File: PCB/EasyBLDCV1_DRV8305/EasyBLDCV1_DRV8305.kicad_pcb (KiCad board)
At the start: 4 copper layers, 66.4 x 43.1 mm, 74 parts, among them J1 10159560-A00221RLF, J2 TC2050-IDC, Q1 CSD16556Q5B, Q2 CSD16556Q5B, Q3 CSD16556Q5B, Q4 CSD16556Q5B, Q5 CSD16556Q5B, Q6 CSD16556Q5B, U1 DRV83053PHP, U2 TMS320F28027FPTT, U3 TPD4E05U06DQAR, U4 LMR16006XDDCR

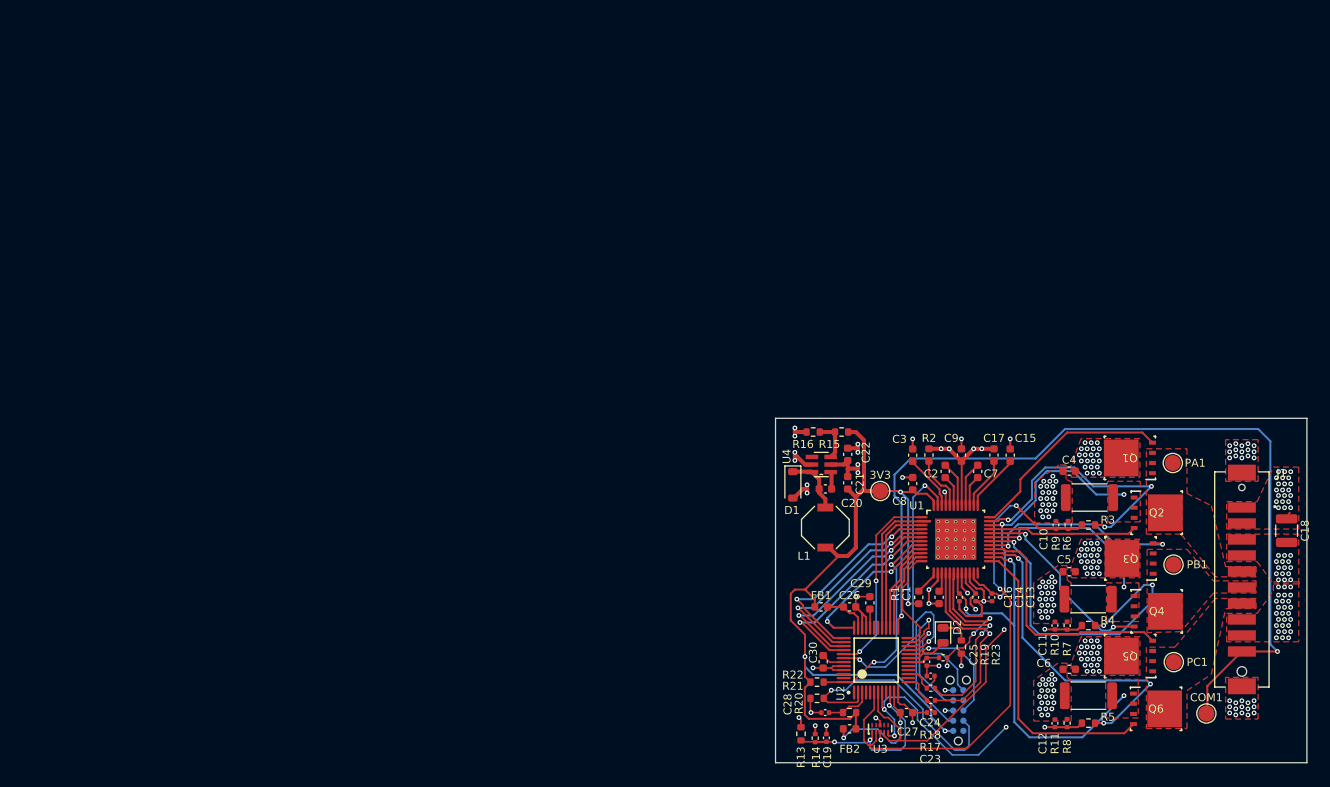
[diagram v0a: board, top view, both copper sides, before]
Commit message: Fixed More DRC started final layout
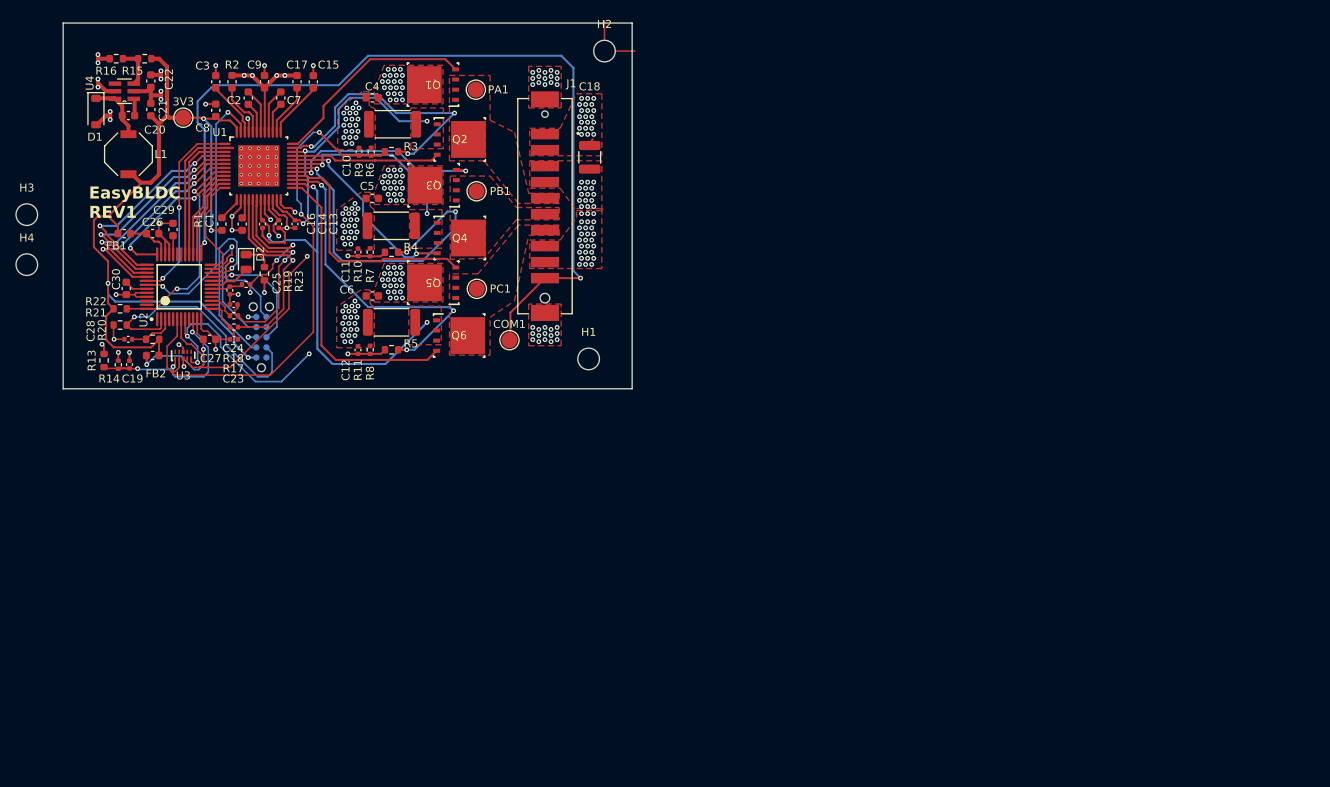
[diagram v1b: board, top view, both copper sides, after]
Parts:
- added H1: M2.5, MountingHole:MountingHole_2.7mm_M2.5_DIN965, F.Cu at (92.6, 70.5)
- added H2: M2.5, MountingHole:MountingHole_2.7mm_M2.5_DIN965, F.Cu at (94.6, 32.0)
- added H3: M2.5, MountingHole:MountingHole_2.7mm_M2.5_DIN965, F.Cu at (22.4, 52.5)
- added H4: M2.5, MountingHole:MountingHole_2.7mm_M2.5_DIN965, F.Cu at (22.4, 58.7)
- moved 3V3 98.8 mm to (41.9, 40.3)
- moved C11 98.8 mm to (63.8, 57.1)
- moved C12 98.8 mm to (63.8, 69.4)
- moved C14 98.8 mm to (53.8, 53.6)
- moved C17 98.8 mm to (58.2, 35.8)
- moved C22 98.8 mm to (37.9, 35.8)
- moved C3 98.8 mm to (46.0, 35.8)
- moved C4 98.8 mm to (65.5, 37.8)
- moved C5 98.8 mm to (65.5, 50.4)
- moved C6 98.8 mm to (65.5, 62.6)
- moved COM1 98.8 mm to (82.7, 68.1)
- moved FB2 98.8 mm to (38.1, 70.1)
- moved J2 98.8 mm to (51.7, 67.8)
- moved L1 98.8 mm to (35.1, 44.9)
- moved PA1 98.8 mm to (78.5, 36.8)
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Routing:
- net GND: track 74.9 -> 76.9 mm, vias 162 -> 163
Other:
- board size 66.4 x 43.1 mm -> 71.1 x 45.7 mm
- board text added: "EasyBLDC REV1"

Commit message: Updated PCB Graphics and Layout
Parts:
- H1, H2, H3, H4: footprint MountingHole:MountingHole_2.7mm_M2.5_DIN965 -> MountingHole:MountingHole_2.7mm_M2.5_ISO7380
- moved H1 74.9 mm to (28.1, 32.4)
- moved H3 72.6 mm to (92.7, 70.4)
- moved H4 13.0 mm to (28.1, 70.4)
- moved C22 3.69 mm to (38.6, 39.4)
- moved C20 3.69 mm to (35.8, 43.7)
- moved C21 3.69 mm to (38.6, 42.9)
- moved D1 3.69 mm to (31.8, 43.2)
- moved L1 3.69 mm to (35.8, 48.5)
- moved R15 3.69 mm to (37.8, 36.6)
- moved R16 3.69 mm to (34.3, 36.6)
- moved U4 3.69 mm to (35.3, 40.6)
- moved H2 1.89 mm to (92.7, 32.4)
- moved 3V3 0.76 mm to (42.7, 40.4)
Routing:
- net 3.3V: track 108.5 -> 105.9 mm
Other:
- board size 71.1 x 45.7 mm -> 72.4 x 45.7 mm

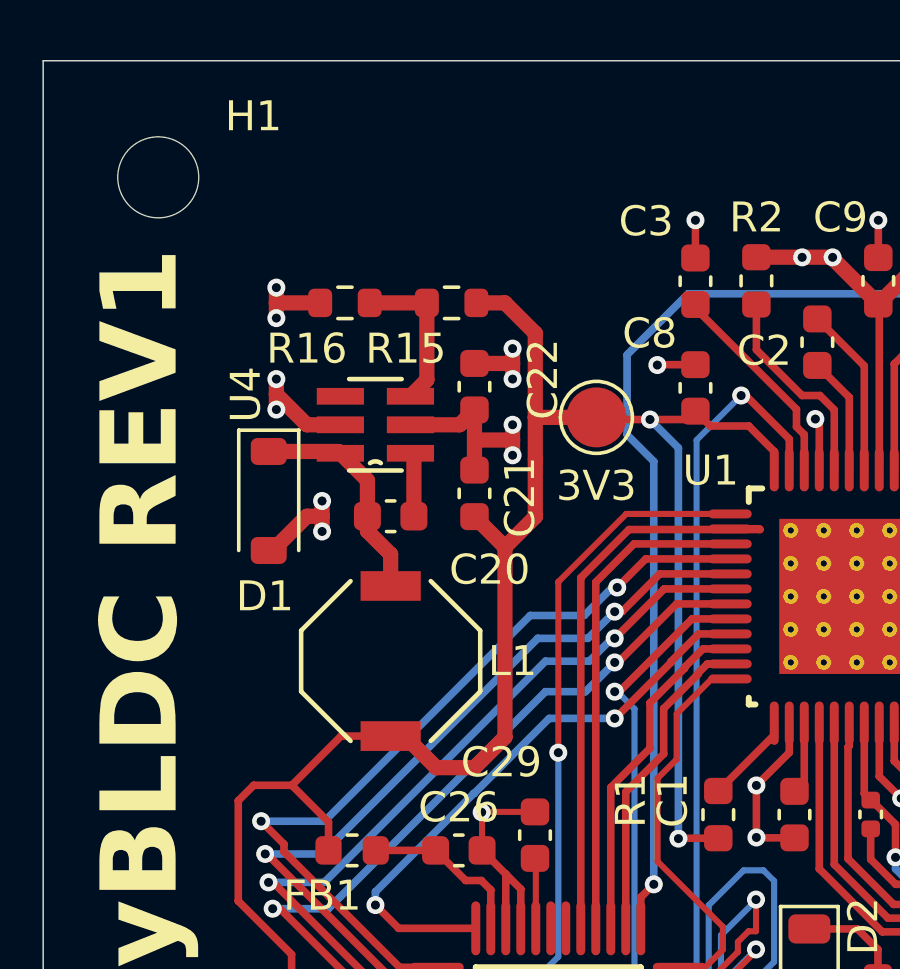
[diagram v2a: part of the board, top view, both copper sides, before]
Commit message: Updated Inductor and excluded tps from BOM
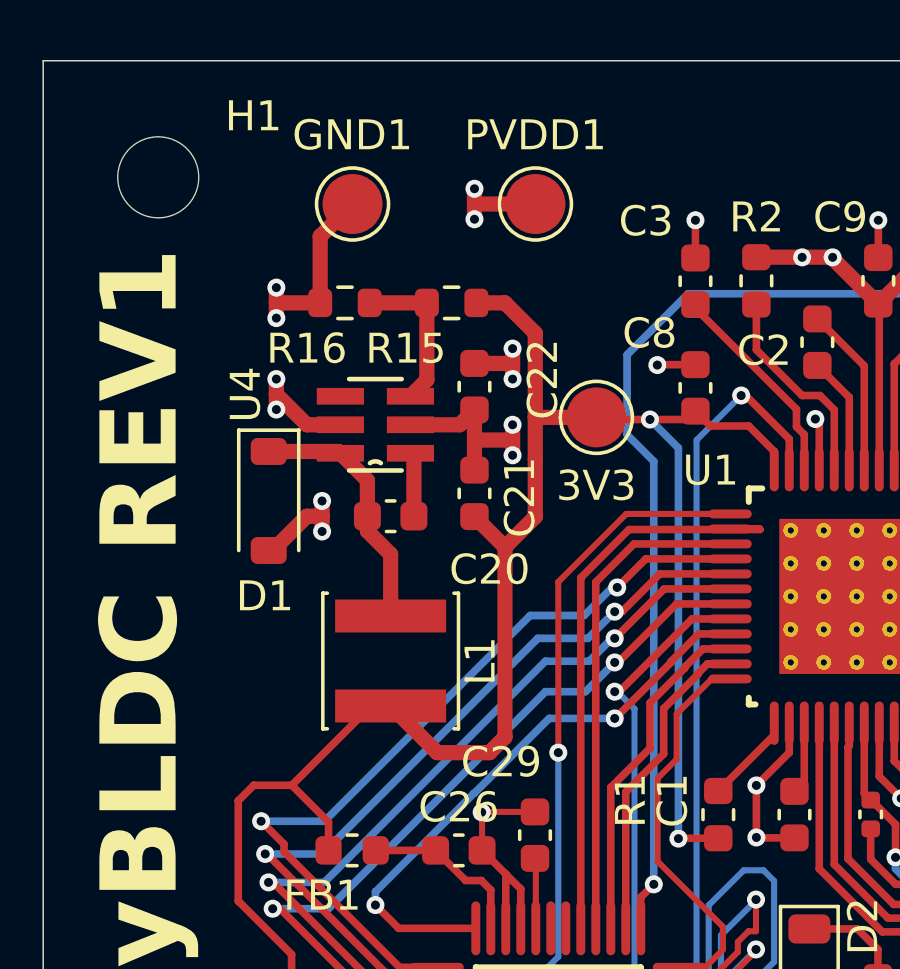
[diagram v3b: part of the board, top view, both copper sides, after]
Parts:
- added GND1: TestPoint, TestPoint:TestPoint_Pad_D2.0mm, F.Cu at (34.5, 33.3)
- added PVDD1: TestPoint, TestPoint:TestPoint_Pad_D2.0mm, F.Cu at (40.6, 33.3)
- L1: footprint EasyBLDC:SD53 -> Inductor_SMD:L_Changjiang_FNR4020S
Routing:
- net GND: track 76.9 -> 80.7 mm
- net PVDD: track 22.4 -> 25.4 mm, vias 93 -> 95
- net Net-(D1-K): track 7.53 -> 8.53 mm

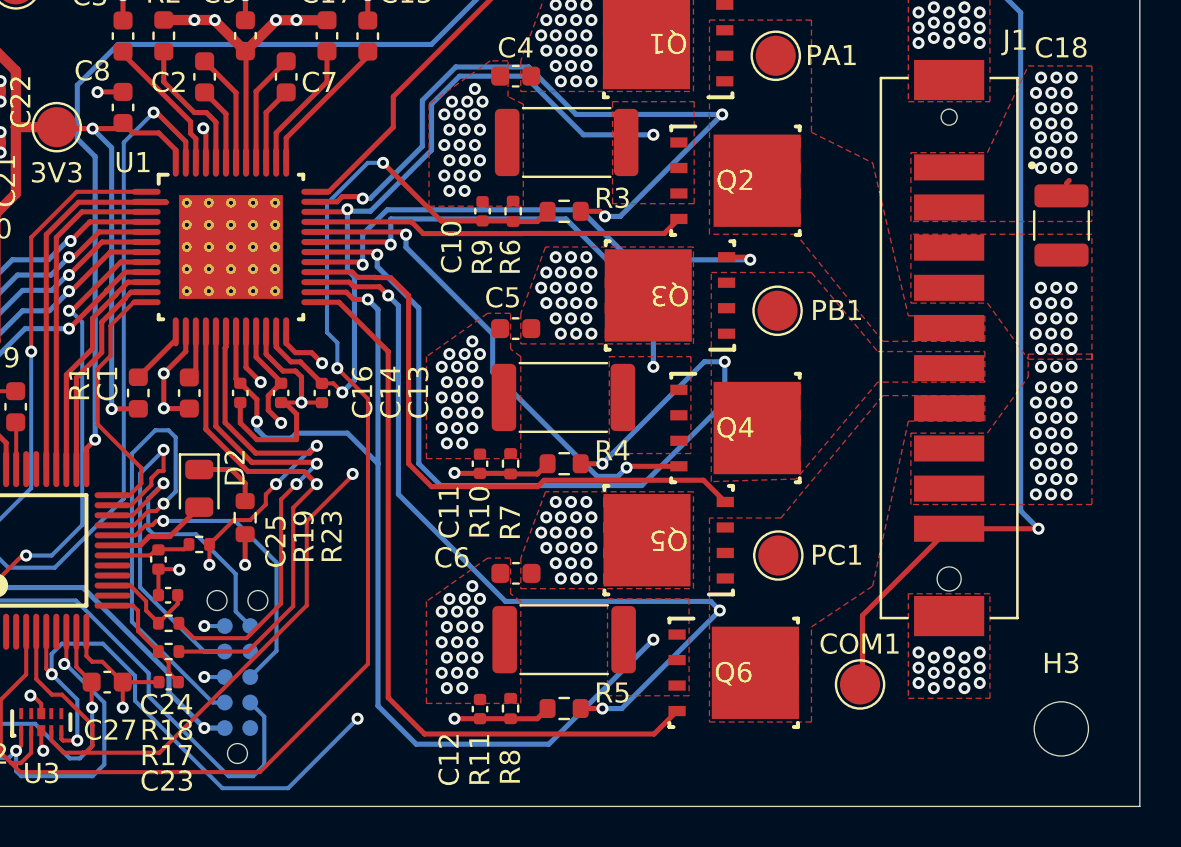
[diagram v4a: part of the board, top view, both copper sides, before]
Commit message: Changed main connector pinout to improve signal integrity
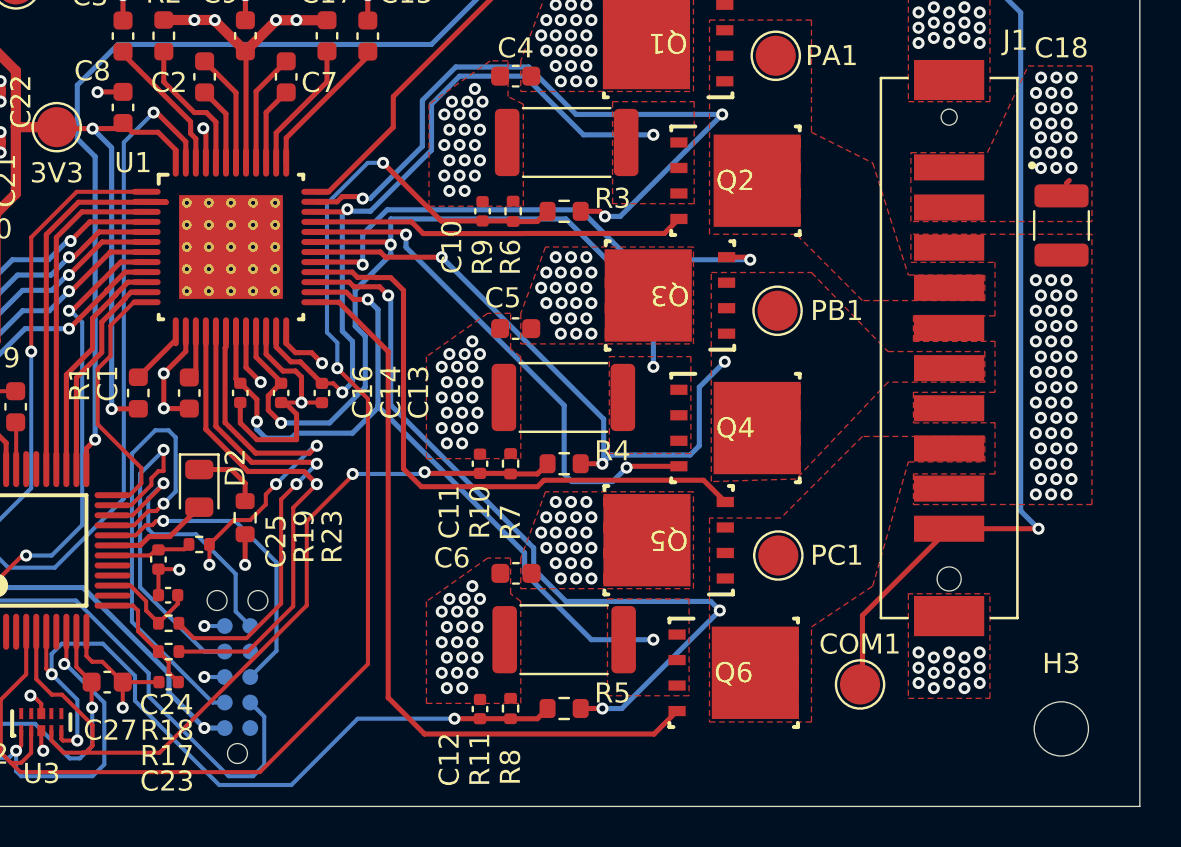
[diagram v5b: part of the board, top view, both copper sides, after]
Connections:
- J1 pad 4: GND -> MOT_A
- J1 pad 5: MOT_A -> GND
- J1 pad 7: MOT_C -> GND
- J1 pad 8: GND -> MOT_C
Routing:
- net SL_C: track 52.1 -> 39.7 mm
- net MOT_B: track 43.1 -> 31.0 mm
- net MOT_C: track 41.4 -> 39.6 mm
- net SL_B: track 42.6 -> 41.5 mm
- net GL_B: track 24.8 -> 25.9 mm
- net VSEN_C: track 38.6 -> 38.4 mm, vias 4 -> 3
- net GND: vias 163 -> 166

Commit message: Fixed Silkscreen DRC Errors
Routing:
- net GND: vias 166 -> 193

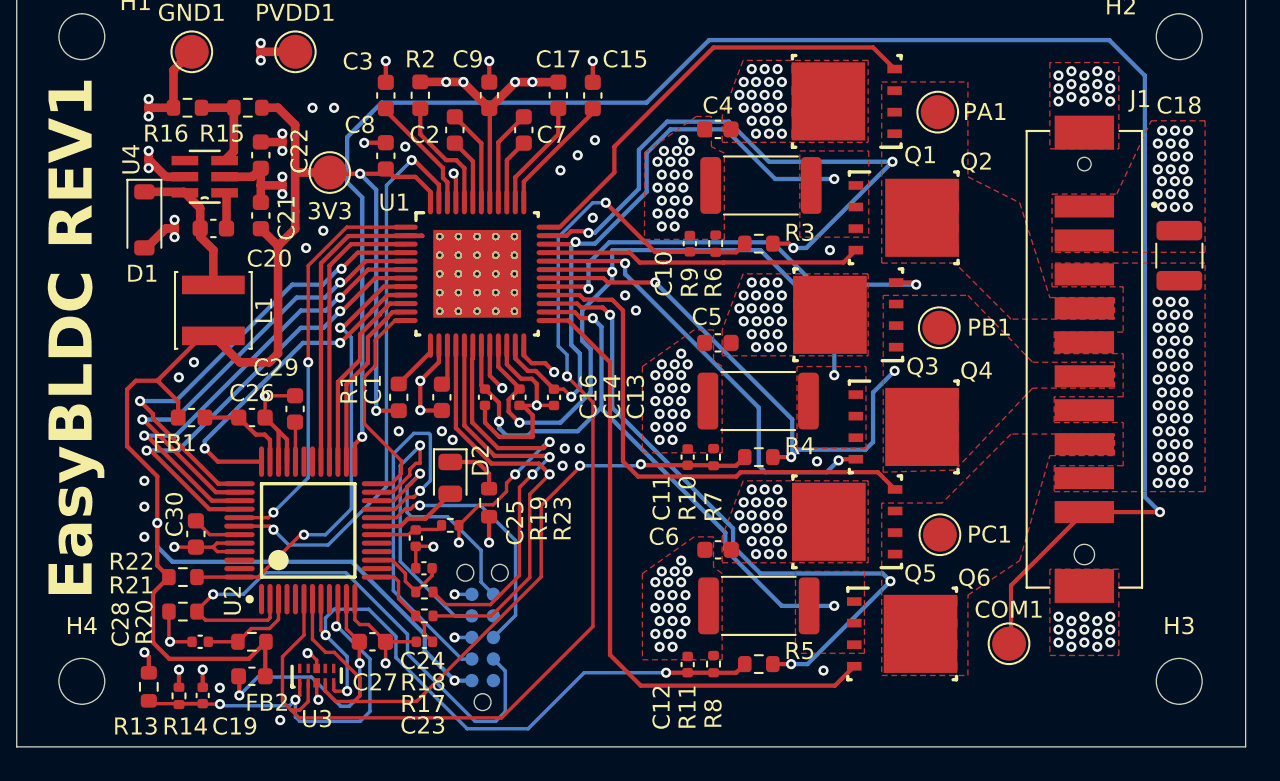
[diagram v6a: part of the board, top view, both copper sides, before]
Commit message: JTAG Connector Changed
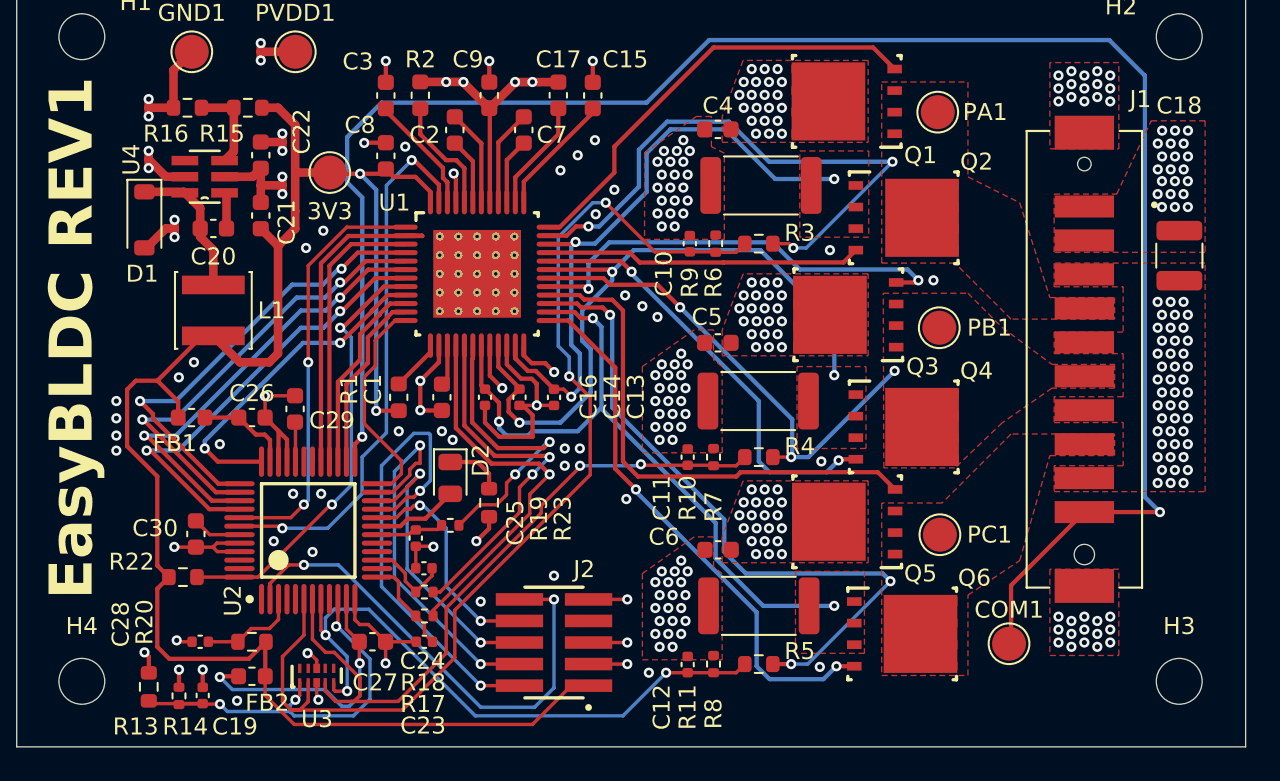
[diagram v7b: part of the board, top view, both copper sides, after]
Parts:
- removed R21: 2.2K, Resistor_SMD:R_0603_1608Metric
- J2: value TC2050-IDC -> FTSH-105-01-F-DV-P-TR; footprint EasyBLDC:Tag-Connect_TC2050-IDC-NL_2x05_P1.27mm_Vertical -> EasyBLDC:SAMTEC_FTSH-105-01-F-DV-P-TR; moved to F.Cu
- moved J2 4.22 mm to (55.9, 68.1)
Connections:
- J2 pad 10: unconnected-(J2-Pin_10-Pad10) -> nTRST
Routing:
- net TCK: track 17.4 -> 22.4 mm, vias 1 -> 2
- net GL_C: track 37.5 -> 32.5 mm, vias 0 -> 2
- net TMS: track 23.6 -> 27.9 mm, vias 1 -> 2
- net VSEN_A: track 66.8 -> 62.6 mm
- net TDO: track 14.0 -> 17.6 mm, vias 1 -> 2
- net nTRST: track 32.7 -> 29.3 mm, vias 1 -> 2
- net GND: track 80.7 -> 83.6 mm, vias 193 -> 204
- net ISEN_B: track 24.3 -> 21.5 mm
- net 3.3V: track 106.1 -> 104.0 mm, vias 4 -> 2
- net TDI: track 15.6 -> 13.5 mm, vias 1 -> 2
- net ISEN_A: track 24.7 -> 22.7 mm
- net MOT_B: track 31.0 -> 29.3 mm
- net WAKE: track 33.6 -> 32.2 mm
- net VSEN_C: track 38.4 -> 37.1 mm
- net ISEN_C: track 18.6 -> 17.7 mm, vias 3 -> 2
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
